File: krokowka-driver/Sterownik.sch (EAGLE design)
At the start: 56 parts, among them IC1 NC7WP14P6X, IC3 NC7WP14P6X, IC4 NC7WP14P6X, T2 N_MOSFET-TO263, T3 N_MOSFET-TO263, T4 N_MOSFET-TO263, T5 N_MOSFET-TO263, T6 N_MOSFET-TO263, T7 N_MOSFET-TO263, T8 N_MOSFET-TO263, T9 N_MOSFET-TO263

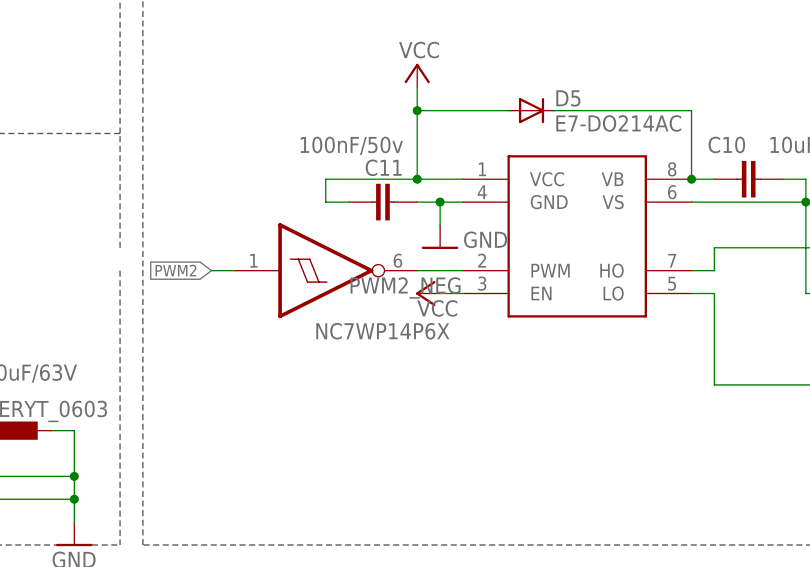
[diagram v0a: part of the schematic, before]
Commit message: poprawilem inwerter invokiem
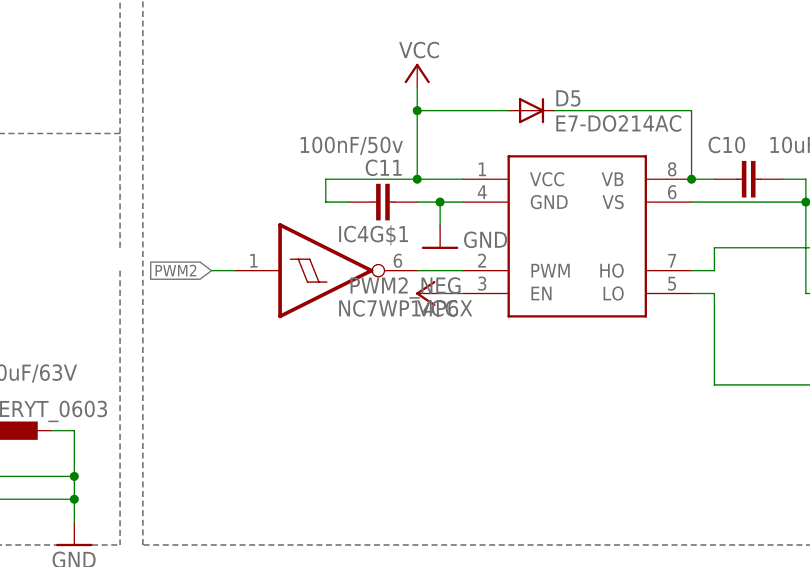
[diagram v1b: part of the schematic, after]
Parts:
- removed IC3: NC7WP14P6X, bufory,invertery:NC7WP14P6X
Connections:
- net PWM2: now also IC4G$1.I; no longer IC3G$1.I
- net PWM2_NEG: now also IC4G$1.O; no longer IC3G$1.O
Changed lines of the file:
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@@
 <?xml version="1.0" encoding="utf-8"?>
 <!DOCTYPE eagle SYSTEM "eagle.dtd">
-<eagle version="7.5.0">
+<eagle version="7.2.0">
 <drawing>
 <settings>
@@
 <grid distance="0.1" unitdist="inch" unit="inch" style="lines" multiple="1" display="no" altdistance="0.01" altunitdist="inch" altunit="inch"/>
 <layers>
-<layer number="1" name="Top" color="4" fill="1" visible="no" active="no"/>
-<layer number="2" name="Route2" color="1" fill="3" visible="no" active="no"/>
-<layer number="3" name="Route3" color="4" fill="3" visible="no" active="no"/>
-<layer number="4" name="Route4" color="1" fill="4" visible="no" active="no"/>
-<layer number="5" name="Route5" color="4" fill="4" visible="no" active="no"/>
-<layer number="6" name="Route6" color="1" fill="8" visible="no" active="no"/>
-<layer number="7" name="Route7" color="4" fill="8" visible="no" active="no"/>
-<layer number="8" name="Route8" color="1" fill="2" visible="no" active="no"/>
-<layer number="9" name="Route9" color="4" fill="2" visible="no" active="no"/>
-<layer number="10" name="Route10" color="1" fill="7" visible="no" active="no"/>
-<layer number="11" name="Route11" color="4" fill="7" visible="no" active="no"/>
-<layer number="12" name="Route12" color="1" fill="5" visible="no" active="no"/>
-<layer number="13" name="Route13" color="4" fill="5" visible="no" active="no"/>
-<layer number="14" name="Route14" color="1" fill="6" visible="no" active="no"/>
-<layer number="15" name="Route15" color="4" fill="6" visible="no" active="no"/>
-<layer number="16" name="Bottom" color="1" fill="1" visible="no" active="no"/>
-<layer number="17" name="Pads" color="2" fill="1" visible="no" active="no"/>
-<layer number="18" name="Vias" color="2" fill="1" visible="no" active="no"/>
-<layer number="19" name="Unrouted" color="6" fill="1" visible="no" active="no"/>
-<layer number="20" name="Dimension" color="15" fill="1" visible="no" active="no"/>
-<layer number="21" name="tPlace" color="7" fill="1" visible="no" active="no"/>
-<layer number="22" name="bPlace" color="7" fill="1" visible="no" active="no"/>
-<layer number="23" name="tOrigins" color="15" fill="1" visible="no" active="no"/>
-<layer number="24" name="bOrigins" color="15" fill="1" visible="no" active="no"/>
-<layer number="25" name="tNames" color="7" fill="1" visible="no" active="no"/>
-<layer number="26" name="bNames" color="7" fill="1" visible="no" active="no"/>
-<layer number="27" name="tValues" color="7" fill="1" visible="no" active="no"/>
-<layer number="28" name="bValues" color="7" fill="1" visible="no" active="no"/>
+<layer number="1" name="Top" color="4" fill="1" visible="yes" active="no"/>
+<layer number="2" name="Route2" color="1" fill="3" visible="yes" active="no"/>
+<layer number="3" name="Route3" color="4" fill="3" visible="yes" active="no"/>
+<layer number="4" name="Route4" color="1" fill="4" visible="yes" active="no"/>
+<layer number="5" name="Route5" color="4" fill="4" visible="yes" active="no"/>
+<layer number="6" name="Route6" color="1" fill="8" visible="yes" active="no"/>
+<layer number="7" name="Route7" color="4" fill="8" visible="yes" active="no"/>
+<layer number="8" name="Route8" color="1" fill="2" visible="yes" active="no"/>
+<layer number="9" name="Route9" color="4" fill="2" visible="yes" active="no"/>
+<layer number="10" name="Route10" color="1" fill="7" visible="yes" active="no"/>
+<layer number="11" name="Route11" color="4" fill="7" visible="yes" active="no"/>
+<layer number="12" name="Route12" color="1" fill="5" visible="yes" active="no"/>
+<layer number="13" name="Route13" color="4" fill="5" visible="yes" active="no"/>
+<layer number="14" name="Route14" color="1" fill="6" visible="yes" active="no"/>
+<layer number="15" name="Route15" color="4" fill="6" visible="yes" active="no"/>
+<layer number="16" name="Bottom" color="1" fill="1" visible="yes" active="no"/>
+<layer number="17" name="Pads" color="2" fill="1" visible="yes" active="no"/>
+<layer number="18" name="Vias" color="2" fill="1" visible="yes" active="no"/>
+<layer number="19" name="Unrouted" color="6" fill="1" visible="yes" active="no"/>
+<layer number="20" name="Dimension" color="15" fill="1" visible="yes" active="no"/>
+<layer number="21" name="tPlace" color="7" fill="1" visible="yes" active="no"/>
+<layer number="22" name="bPlace" color="7" fill="1" visible="yes" active="no"/>
+<layer number="23" name="tOrigins" color="15" fill="1" visible="yes" active="no"/>
+<layer number="24" name="bOrigins" color="15" fill="1" visible="yes" active="no"/>
+<layer number="25" name="tNames" color="7" fill="1" visible="yes" active="no"/>
+<layer number="26" name="bNames" color="7" fill="1" visible="yes" active="no"/>
+<layer number="27" name="tValues" color="7" fill="1" visible="yes" active="no"/>
+<layer number="28" name="bValues" color="7" fill="1" visible="yes" active="no"/>
 <layer number="29" name="tStop" color="7" fill="3" visible="no" active="no"/>
 <layer number="30" name="bStop" color="7" fill="6" visible="no" active="no"/>
@@
 <layer number="35" name="tGlue" color="7" fill="4" visible="no" active="no"/>
 <layer number="36" name="bGlue" color="7" fill="5" visible="no" active="no"/>
-<layer number="37" name="tTest" color="7" fill="1" visible="no" active="no"/>
-<layer number="38" name="bTest" color="7" fill="1" visible="no" active="no"/>
+<layer number="37" name="tTest" color="7" fill="1" visible="yes" active="no"/>
+<layer number="38" name="bTest" color="7" fill="1" visible="yes" active="no"/>
 <layer number="39" name="tKeepout" color="4" fill="11" visible="no" active="no"/>
 <layer number="40" name="bKeepout" color="1" fill="11" visible="no" active="no"/>
@@
 <layer number="44" name="Drills" color="7" fill="1" visible="no" active="no"/>
 <layer number="45" name="Holes" color="7" fill="1" visible="no" active="no"/>
-<layer number="46" name="Milling" color="3" fill="1" visible="no" active="no"/>
-<layer number="47" name="Measures" color="7" fill="1" visible="no" active="no"/>
-<layer number="48" name="Document" color="7" fill="1" visible="no" active="no"/>
-<layer number="49" name="Reference" color="7" fill="1" visible="no" active="no"/>
-<layer number="50" name="dxf" color="7" fill="1" visible="no" active="no"/>
-<layer number="51" name="tDocu" color="7" fill="1" visible="no" active="no"/>
-<layer number="52" name="bDocu" color="7" fill="1" visible="no" active="no"/>
-<layer number="56" name="wert" color="7" fill="1" visible="no" active="no"/>
+<layer number="46" name="Milling" color="3" fill="1" visible="yes" active="no"/>
+<layer number="47" name="Measures" color="7" fill="1" visible="yes" active="no"/>
+<layer number="48" name="Document" color="7" fill="1" visible="yes" active="no"/>
+<layer number="49" name="Reference" color="7" fill="1" visible="yes" active="no"/>
+<layer number="50" name="dxf" color="7" fill="1" visible="yes" active="no"/>
+<layer number="51" name="tDocu" color="7" fill="1" visible="yes" active="no"/>
+<layer number="52" name="bDocu" color="7" fill="1" visible="yes" active="no"/>
+<layer number="56" name="wert" color="7" fill="1" visible="yes" active="no"/>
 <layer number="90" name="Modules" color="5" fill="1" visible="yes" active="yes"/>
 <layer number="91" name="Nets" color="2" fill="1" visible="yes" active="yes"/>
@@
 <part name="GND13" library="robione" deviceset="GND" device=""/>
 <part name="U$3" library="fuse" deviceset="FUSE0603" device=""/>
-<part name="IC3" library="bufory,invertery" deviceset="NC7W*14" device="P6X" technology="P"/>
 <part name="IC4" library="bufory,invertery" deviceset="NC7W*14" device="P6X" technology="P"/>
 <part name="D1" library="diode" deviceset="E7-DO214AC" device=""/>
@@
 <attribute name="VALUE" x="-13.97" y="65.659" size="1.778" layer="96"/>
 </instance>
-<instance part="IC3" gate="G$1" x="35.56" y="-2.54" smashed="yes">
-<attribute name="VALUE" x="34.29" y="-10.16" size="1.778" layer="96" font="vector"/>
-</instance>
 <instance part="IC4" gate="G$2" x="149.86" y="-2.54" smashed="yes">
 <attribute name="VALUE" x="148.59" y="-10.16" size="1.778" layer="96" font="vector"/>
@@
 <instance part="U$5" gate="G$1" x="-71.12" y="38.1"/>
 <instance part="IC4" gate="G$3" x="-63.5" y="-10.16" smashed="yes"/>
+<instance part="IC4" gate="G$1" x="35.56" y="-2.54"/>
 </instances>
 <busses>
@@
 </segment>
 <segment>
-<pinref part="IC3" gate="G$1" pin="I"/>
 <wire x1="25.4" y1="-2.54" x2="22.86" y2="-2.54" width="0.1524" layer="91"/>
 <label x="22.86" y="-2.54" size="1.27" layer="95" rot="R180" xref="yes"/>
+<pinref part="IC4" gate="G$1" pin="I"/>
 </segment>
 </net>
@@
 <net name="PWM2_NEG" class="0">
 <segment>
-<pinref part="IC3" gate="G$1" pin="O"/>
 <pinref part="U$18" gate="G$1" pin="PWM"/>
 <wire x1="45.72" y1="-2.54" x2="50.8" y2="-2.54" width="0.1524" layer="91"/>
 <label x="38.1" y="-5.08" size="1.778" layer="95"/>
-</segment>
-<segment>
+<pinref part="IC4" gate="G$1" pin="O"/>
+</segment>
+<segment>
